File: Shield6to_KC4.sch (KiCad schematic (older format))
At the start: 33 parts, among them J1 DB9, P1 CONN_9, P2 CONN_8, P3 CONN_9, P4 CONN_8, P5 CONN_8, P6 CONN_8, P7 CONN_8, P8 CONN_8, SW1 SW_PUSH, SW2 SW_PUSH, SW3 SW_PUSH, SW4 SW_PUSH, U1 ID-12LA, U2 MAX232

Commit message: Changes to be committed: 	renamed:    Librerias.pretty/ID12-LA.kicad_mod -> Modulos/ID12-LA.kicad_mod 	modified:   Shield6to_KC4-cache.lib 	renamed:    _saved_Shield6to_KC4.sch -> Shield6to_KC4.bak 	modified:   Shield6to_KC4.net 	modified:   Shield6to_KC4.sch 	renamed:    Shield6to_KC4_sin_conectores.kicad_pcb -> Shield6to_KC4_Con_RFID.kicad_pcb 	renamed:    Shield6to_KC4.kicad_pcb -> Shield6to_KC4_SinRFID.kicad_pcb 	modified:   Shield6to_KC4_sin_conectores.kicad_pcb-bak 	new file:   Shield6to_KC4_sin_conectores.pro 	deleted:    Shield6to_KICAD4.net 	renamed:    Shield6to_KC4+.kicad_pcb -> _autosave-Shield6to_KC4_sin_conectores.kicad_pcb
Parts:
- removed P6, P7: CONN_8, Socket_Strips:Socket_Strip_Straight_1x08, symbol CONN_8
- added R6: 1K, Resistors_ThroughHole:Resistor_Horizontal_RM10mm, symbol R
- added R7: 10K, Resistors_ThroughHole:Resistor_Horizontal_RM10mm, symbol R
- added SW5: RESET, Buttons_Switches_ThroughHole:SW_PUSH_SMALL, symbol SW_PUSH
- JP3: footprint Pin_Headers:Pin_Header_Angled_1x03 -> Pin_Headers:Pin_Header_Straight_1x03
- R1, R2, R3, R4: value R -> 10K
- R5: value R -> 3K3
- SW1: value SW_PUSH -> BOOT
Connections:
- wire segments 124 -> 94
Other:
- moved on the sheet: D1, JP1, JP2, JP3, P1, P2, P3, P4, P5, P8, R5, RV1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

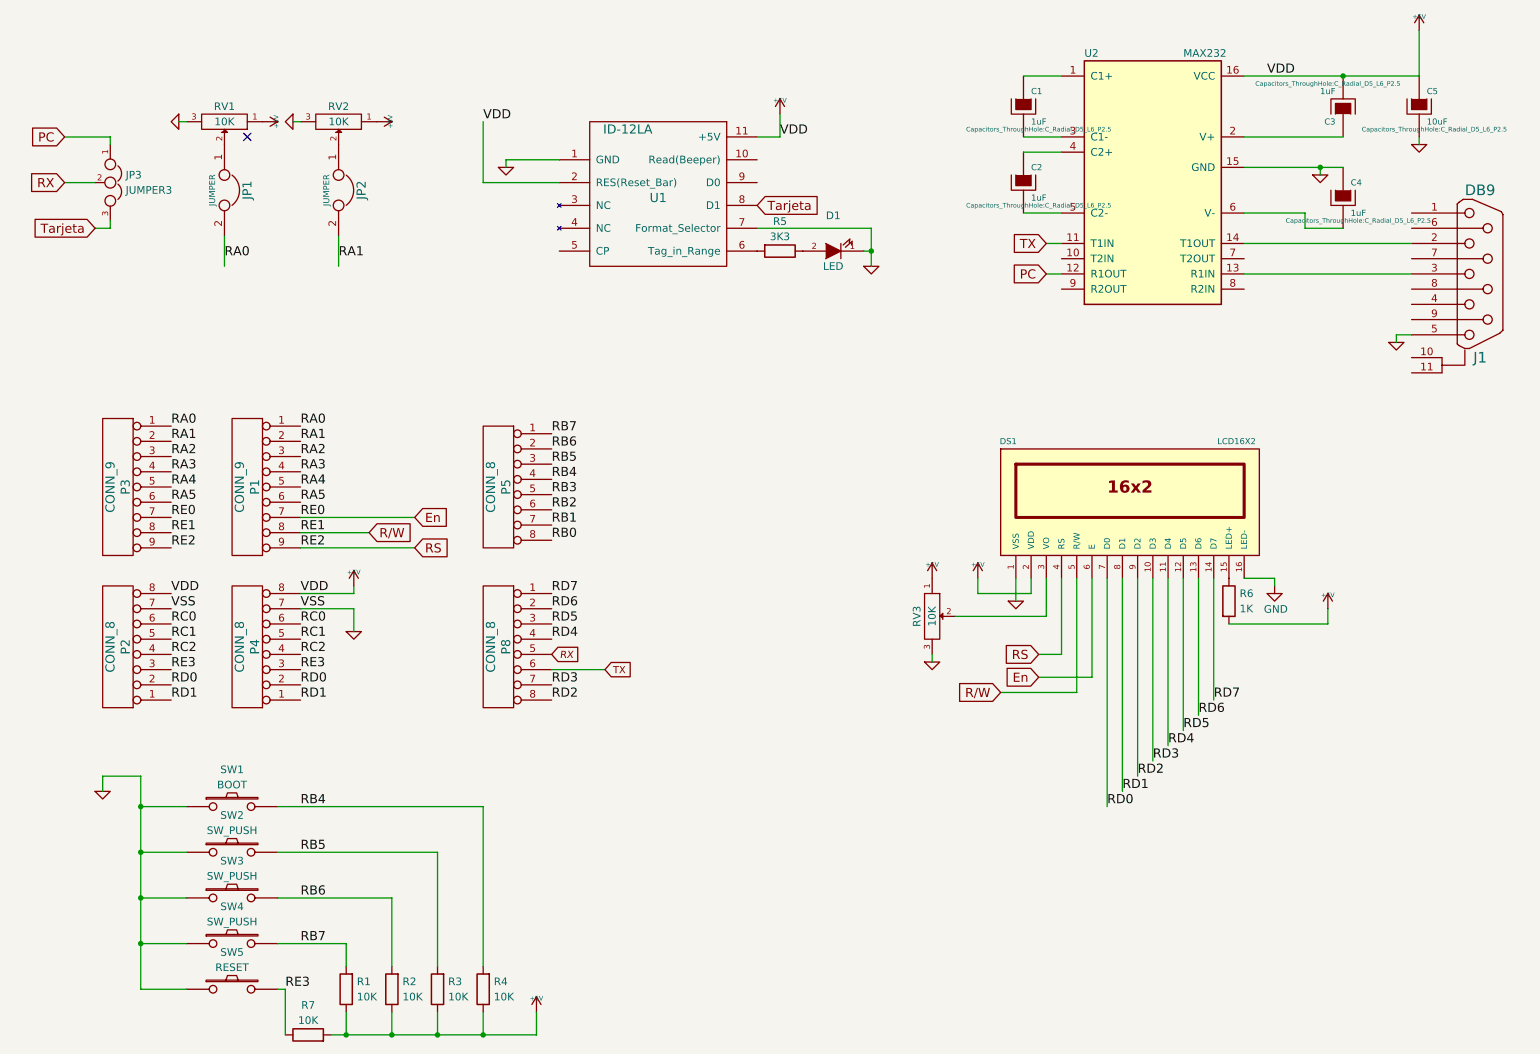
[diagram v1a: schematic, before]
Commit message: Committer: Esteban Lemos <esteban@mobile.lemos>
 On branch master
 Your branch is up-to-date with 'origin/master'.

 Changes to be committed:
	deleted:    Shield6to.kicad_pcb_sin_micro_1.kicad_pcb-bak
	deleted:    Shield6to.kicad_pcb_sin_micro_1.pro
	deleted:    Shield6to.pro
	modified:   Shield6to_KC4.bak
	renamed:    Shield6to_KC4_Con_RFID.kicad_pcb -> Shield6to_KC4.kicad_pcb
	deleted:    Shield6to_KC4.kicad_pcb-bak
	modified:   Shield6to_KC4.net
	modified:   Shield6to_KC4.pro
	modified:   Shield6to_KC4.sch
	deleted:    Shield6to_KC4_Con_RFID.kicad_pcb-bak
	deleted:    Shield6to_KC4_Con_RFID.pro
	deleted:    Shield6to_KC4_SinRFID.pro
	deleted:    Shield6to_KC4_sin_conectores.kicad_pcb-bak
	deleted:    Shield6to_KC4_sin_conectores.pro
	deleted:    _autosave-Shield6to_KC4.kicad_pcb
	deleted:    _autosave-Shield6to_KC4_sin_conectores.kicad_pcb
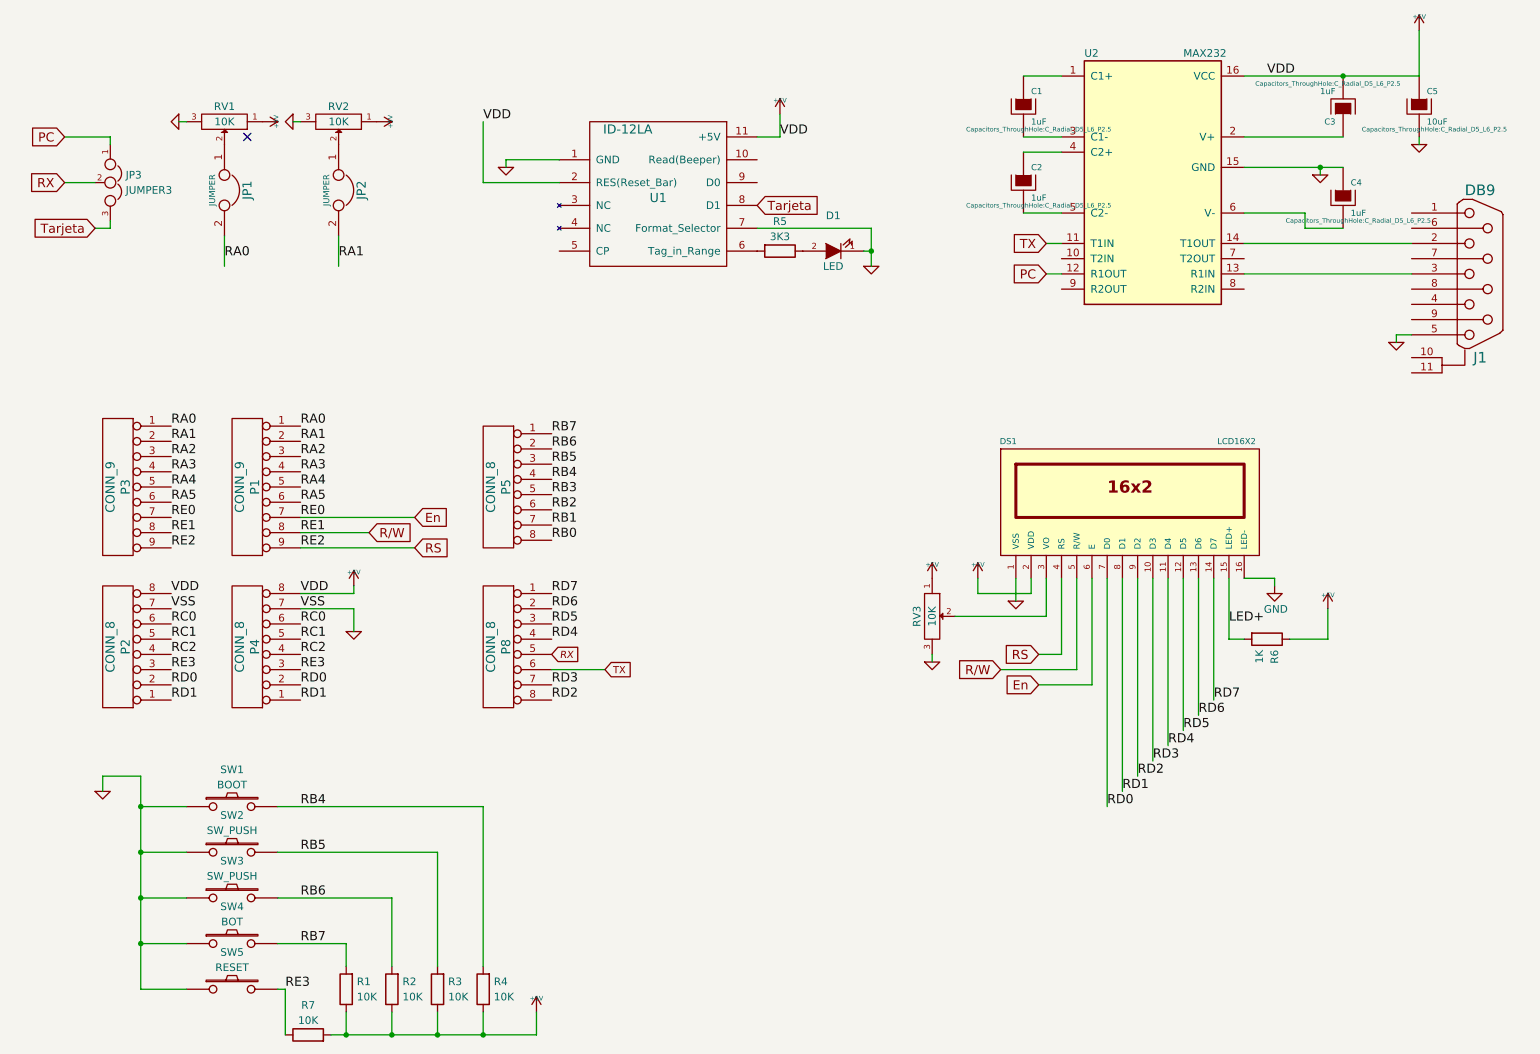
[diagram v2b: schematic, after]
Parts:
- SW4: value SW_PUSH -> BOT
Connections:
- net +5V: now also R6.1; no longer R6.2
- net LED+: now reaches DS1.15 (LED+)
- net LED+: now also R6.2; no longer R6.1
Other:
- moved on the sheet: R6
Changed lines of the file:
@@
 	1    0    0    -1
 $EndComp
-Text GLabel 7650 5150 0    60   Input ~ 0
+Text GLabel 7650 5200 0    60   Input ~ 0
 En
 Text GLabel 7650 5000 0    60   Input ~ 0
@@
 	7800 5000 7800 4500
 Wire Wire Line
-	7650 5150 8000 5150
-Wire Wire Line
-	8000 5150 8000 4500
+	7650 5200 8000 5200
+Wire Wire Line
+	8000 5200 8000 4500
 Text GLabel 3550 4100 2    60   Input ~ 0
 En
 Text GLabel 3550 4300 2    60   Input ~ 0
 RS
-Text GLabel 7400 5250 0    60   Input ~ 0
+Text GLabel 7400 5100 0    60   Input ~ 0
 R/W
 Wire Wire Line
-	7400 5250 7900 5250
-Wire Wire Line
-	7900 5250 7900 4500
+	7400 5100 7900 5100
+Wire Wire Line
+	7900 5100 7900 4500
 Text GLabel 3250 4200 2    60   Input ~ 0
 R/W
@@
 P 2350 6900
 F 0 "SW4" H 2350 7143 50  0000 C CNN
-F 1 "SW_PUSH" H 2350 7043 50  0000 C CNN
+F 1 "BOT" H 2350 7043 50  0000 C CNN
 F 2 "Buttons_Switches_ThroughHole:SW_PUSH_SMALL" H 2350 6900 50  0001 C CNN
 F 3 "" H 2350 6900 50  0000 C CNN
@@
 L R R6
 U 1 1 5679C878
-P 8900 4650
-F 0 "R6" H 8970 4700 50  0000 L CNN
-F 1 "1K" H 8970 4600 50  0000 L CNN
-F 2 "Resistors_ThroughHole:Resistor_Horizontal_RM10mm" V 8830 4650 50  0001 C CNN
-F 3 "" H 8900 4650 50  0000 C CNN
-	1    8900 4650
-	1    0    0    -1
-$EndComp
-Wire Wire Line
-	8900 4800 9550 4800
+P 9150 4900
+F 0 "R6" H 9220 4950 50  0000 L CNN
+F 1 "1K" H 9220 4850 50  0000 L CNN
+F 2 "Resistors_ThroughHole:Resistor_Horizontal_RM10mm" V 9080 4900 50  0001 C CNN
+F 3 "" H 9150 4900 50  0000 C CNN
+	1    9150 4900
+	0    1    1    0
+$EndComp
+Wire Wire Line
+	9550 4700 9550 4900
 $Comp
 L GND #PWR020
@@
 	1    0    0    -1
 $EndComp
-Wire Wire Line
-	9550 4800 9550 4700
 $Comp
 L SW_PUSH SW5
@@
 Text Label 8800 5300 0    60   ~ 0
 RD7
+Text Label 8900 4800 0    60   ~ 0
+LED+
+Wire Wire Line
+	9550 4900 9300 4900
+Wire Wire Line
+	9000 4900 8900 4900
+Wire Wire Line
+	8900 4900 8900 4500
 $EndSCHEMATC

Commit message: On branch master  Your branch is up-to-date with 'origin/master'.
 Changes to be committed:
	modified:   Shield6to_KC4.bak
	modified:   Shield6to_KC4.kicad_pcb
	modified:   Shield6to_KC4.kicad_pcb-bak
	modified:   Shield6to_KC4.net
	modified:   Shield6to_KC4.sch
	deleted:    _saved_Shield6to_KC4.sch
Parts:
- removed R5: 3K3, Resistors_ThroughHole:Resistor_Horizontal_RM10mm, symbol R
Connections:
- net RC0: now also P2.5 (P5), P4.5 (P5); no longer P2.6 (P6), P4.6 (P6)
- net RC1: now also P2.4 (P4), P4.4 (P4); no longer P2.5 (P5), P4.5 (P5)
- net RC2: now also P2.3 (P3), P4.3 (P3); no longer P2.4 (P4), P4.4 (P4)
- net RE3: now also P2.6 (P6), P4.6 (P6); no longer P2.3 (P3), P4.3 (P3)
- net at U1.6 (Tag_in_Range): now also D1.2 (A)
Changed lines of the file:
@@
 Text Label 1950 4300 0    60   ~ 0
 RE2
-Text Label 2800 5100 0    60   ~ 0
+Text Label 2800 4800 0    60   ~ 0
 RE3
 Text Label 3050 2400 0    60   ~ 0
@@
 Text Label 2300 2400 0    60   ~ 0
 RA0
-Text Label 2800 4800 0    60   ~ 0
+Text Label 2800 4900 0    60   ~ 0
 RC0
-Text Label 2800 4900 0    60   ~ 0
+Text Label 2800 5000 0    60   ~ 0
 RC1
-Text Label 2800 5000 0    60   ~ 0
+Text Label 2800 5100 0    60   ~ 0
 RC2
 Text Label 2800 4600 0    60   ~ 0
@@
 VDD
 $Comp
-L R R5
-U 1 1 5676C37D
-P 5950 2350
-F 0 "R5" V 5755 2350 50  0000 C CNN
-F 1 "3K3" V 5855 2350 50  0000 C CNN
-F 2 "Resistors_ThroughHole:Resistor_Horizontal_RM10mm" V 5880 2350 50  0001 C CNN
-F 3 "" H 5950 2350 50  0000 C CNN
-	1    5950 2350
-	0    1    1    0
-$EndComp
-$Comp
 L GND-RESCUE-Shield6to #PWR019
 U 1 1 5676C416
@@
 Text Label 1950 4700 0    60   ~ 0
 VSS
+Text Label 1950 4900 0    60   ~ 0
+RC0
+Text Label 1950 5000 0    60   ~ 0
+RC1
+Text Label 1950 5100 0    60   ~ 0
+RC2
 Text Label 1950 4800 0    60   ~ 0
-RC0
-Text Label 1950 4900 0    60   ~ 0
-RC1
-Text Label 1950 5000 0    60   ~ 0
-RC2
-Text Label 1950 5100 0    60   ~ 0
 RE3
 Text Label 1950 5200 0    60   ~ 0
@@
 Wire Wire Line
 	8900 4900 8900 4500
+Wire Wire Line
+	5800 2350 6100 2350
 $EndSCHEMATC

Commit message: Changes to be committed: 	new file:   3d_indicators.zip 	new file:   Modelodelgabinete.fcstd 	new file:   Modelodelgabinete.fcstd1 	modified:   Shield6to_KC4.bak 	modified:   Shield6to_KC4.kicad_pcb 	modified:   Shield6to_KC4.kicad_pcb-bak 	modified:   Shield6to_KC4.net 	modified:   Shield6to_KC4.sch 	new file:   box.pro 	new file:   box.stl 	new file:   placaFreeCad.fcstd
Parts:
- SW1: value BOOT -> BOOT/BOT1
- SW2: value SW_PUSH -> BOT2
- SW3: value SW_PUSH -> BOT3
- SW4: value BOT -> BOT4
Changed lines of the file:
@@
 P 2350 6000
 F 0 "SW1" H 2350 6243 50  0000 C CNN
-F 1 "BOOT" H 2350 6143 50  0000 C CNN
+F 1 "BOOT/BOT1" H 2350 6143 50  0000 C CNN
 F 2 "Buttons_Switches_ThroughHole:SW_PUSH_SMALL" H 2350 6000 50  0001 C CNN
 F 3 "" H 2350 6000 50  0000 C CNN
@@
 P 2350 6300
 F 0 "SW2" H 2350 6543 50  0000 C CNN
-F 1 "SW_PUSH" H 2350 6443 50  0000 C CNN
+F 1 "BOT2" H 2350 6443 50  0000 C CNN
 F 2 "Buttons_Switches_ThroughHole:SW_PUSH_SMALL" H 2350 6300 50  0001 C CNN
 F 3 "" H 2350 6300 50  0000 C CNN
@@
 P 2350 6600
 F 0 "SW3" H 2350 6843 50  0000 C CNN
-F 1 "SW_PUSH" H 2350 6743 50  0000 C CNN
+F 1 "BOT3" H 2350 6743 50  0000 C CNN
 F 2 "Buttons_Switches_ThroughHole:SW_PUSH_SMALL" H 2350 6600 50  0001 C CNN
 F 3 "" H 2350 6600 50  0000 C CNN
@@
 P 2350 6900
 F 0 "SW4" H 2350 7143 50  0000 C CNN
-F 1 "BOT" H 2350 7043 50  0000 C CNN
+F 1 "BOT4" H 2350 7043 50  0000 C CNN
 F 2 "Buttons_Switches_ThroughHole:SW_PUSH_SMALL" H 2350 6900 50  0001 C CNN
 F 3 "" H 2350 6900 50  0000 C CNN

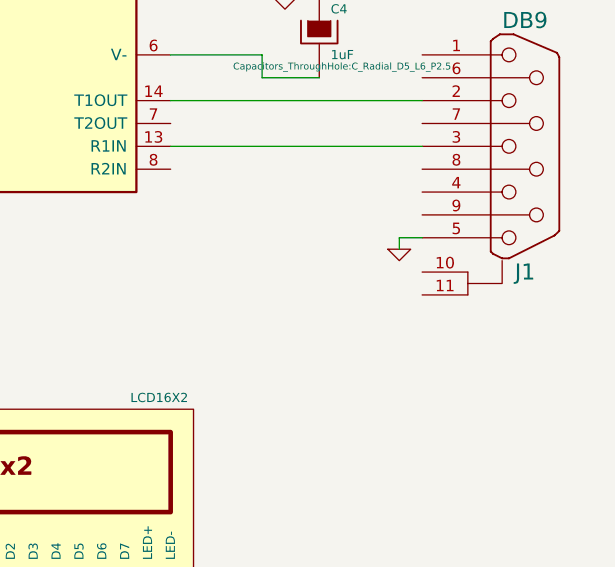
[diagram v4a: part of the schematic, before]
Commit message: Changes to be committed: 	modified:   Modelodelgabinete.fcstd 	modified:   Modelodelgabinete.fcstd1 	new file:   Modelodelgabinete3.fcstd 	new file:   Modelodelgabinete4.fcstd 	new file:   Modelodelgabinete4.fcstd1 	new file:   Modelodelgabinete5.fcstd 	new file:   Modelodelgabinete5.fcstd1 	new file:   ProbandoFreecad17.fcstd 	new file:   ProbandoFreecad17.fcstd1 	modified:   Shield6to_KC4-cache.lib 	modified:   Shield6to_KC4.bak 	modified:   Shield6to_KC4.kicad_pcb 	modified:   Shield6to_KC4.kicad_pcb-bak 	modified:   Shield6to_KC4.sch 	new file:   box2.stl 	new file:   box3.pro 	new file:   box3.stl 	new file:   box_Rev1.stl
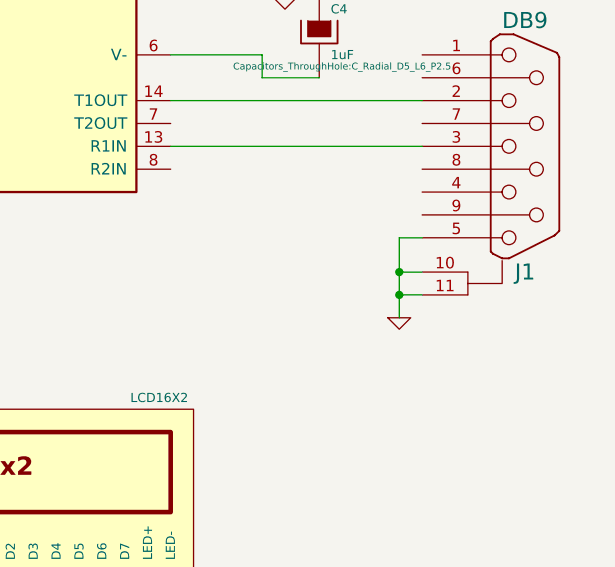
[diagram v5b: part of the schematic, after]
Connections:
- net GND: now also J1.10 (GND), J1.11 (GND)
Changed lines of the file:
@@
 L GND-RESCUE-Shield6to #PWR03
 U 1 1 56644E4B
-P 10000 2950
-F 0 "#PWR03" H 10000 2950 30  0001 C CNN
-F 1 "GND" H 10000 2880 30  0001 C CNN
-F 2 "" H 10000 2950 60  0000 C CNN
-F 3 "" H 10000 2950 60  0000 C CNN
-	1    10000 2950
+P 10000 3250
+F 0 "#PWR03" H 10000 3250 30  0001 C CNN
+F 1 "GND" H 10000 3180 30  0001 C CNN
+F 2 "" H 10000 3250 60  0000 C CNN
+F 3 "" H 10000 3250 60  0000 C CNN
+	1    10000 3250
 	1    0    0    -1
 $EndComp
@@
 	10000 2900 10100 2900
 Wire Wire Line
-	10000 2950 10000 2900
+	10000 2900 10000 3250
 Wire Wire Line
 	10150 1600 10150 1650
@@
 Wire Wire Line
 	5800 2350 6100 2350
+Wire Wire Line
+	10100 3050 10000 3050
+Connection ~ 10000 3050
+Wire Wire Line
+	10100 3150 10000 3150
+Connection ~ 10000 3150
 $EndSCHEMATC
